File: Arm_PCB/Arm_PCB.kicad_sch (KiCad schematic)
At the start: 29 parts, among them J1 Conn_02x02_Counter_Clockwise, J10 Conn_02x04_Counter_Clockwise, J11 Conn_02x04_Counter_Clockwise, J2 Conn_02x03_Counter_Clockwise, J3 Conn_02x07_Counter_Clockwise, J4 Conn_02x05_Counter_Clockwise, J5 Conn_02x04_Counter_Clockwise, J6 Conn_02x04_Counter_Clockwise, J7 Conn_02x04_Counter_Clockwise, J8 Conn_02x04_Counter_Clockwise, J9 Conn_02x02_Counter_Clockwise, SW0 SW_Push, SW1 SW_Push, SW2 SW_Push, SW3 SW_Push

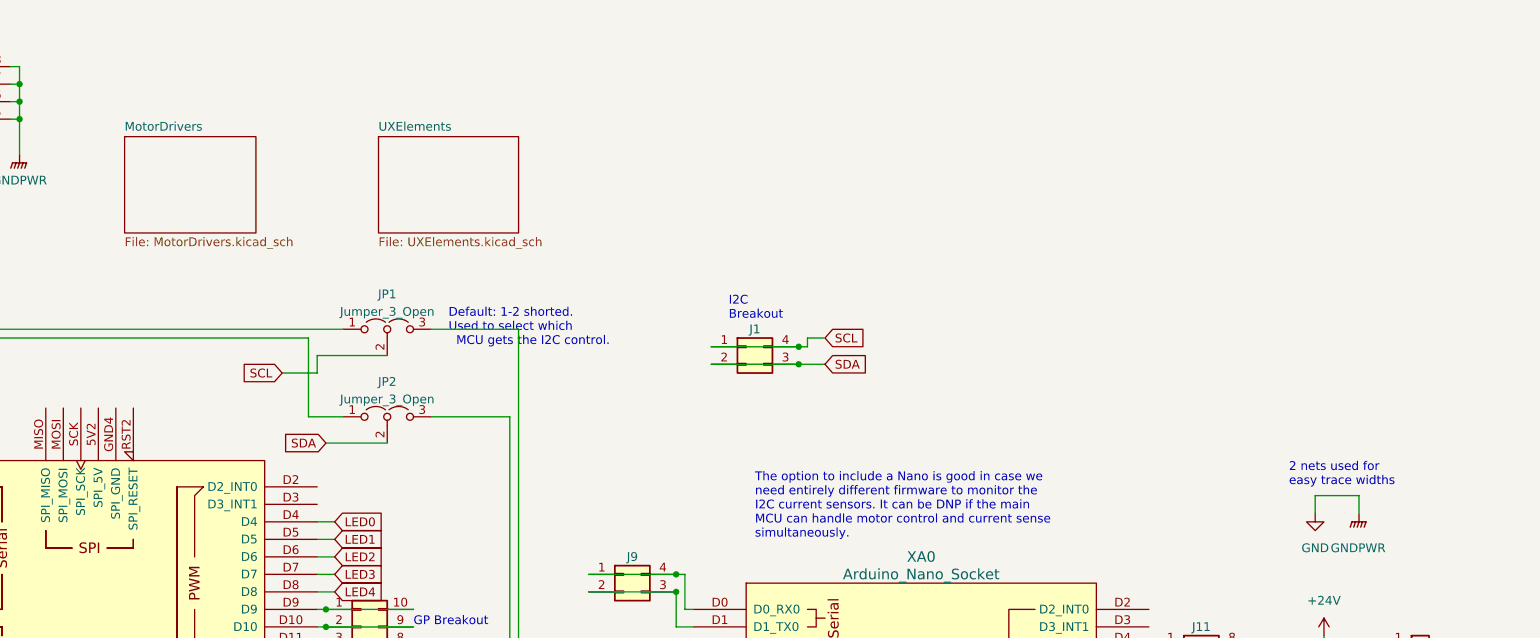
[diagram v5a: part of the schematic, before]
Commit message: Add servo current sensors, etc.
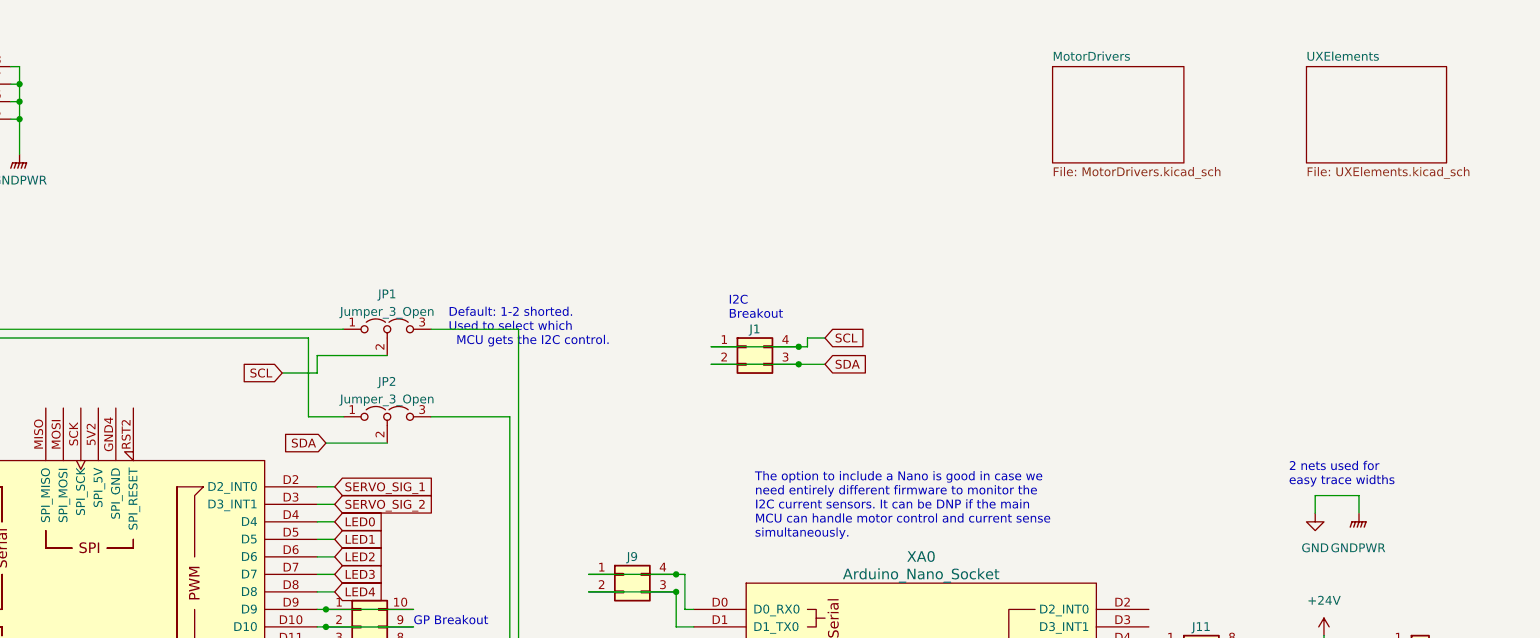
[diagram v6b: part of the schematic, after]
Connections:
- net SERVO_SIG_1: now reaches XA1.D2 (D2_INT0)
- net SERVO_SIG_2: now reaches XA1.D3 (D3_INT1)
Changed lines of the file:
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@@
+    (stroke (width 0) (type default))
+  )
+  (wire (pts (xy 93.98 82.55) (xy 96.52 82.55))
     (stroke (width 0) (type default))
   )
@@
   )
   (wire (pts (xy 13.97 87.63) (xy 26.67 87.63))
+    (stroke (width 0) (type default))
+  )
+  (wire (pts (xy 93.98 85.09) (xy 96.52 85.09))
     (stroke (width 0) (type default))
   )
@@
     (effects (font (size 1.27 1.27)) (justify left))
     (property "Intersheetrefs" "${INTERSHEET_REFS}" (at 105.0412 120.5706 0)
+      (effects (font (size 1.27 1.27)) (justify left) hide)
+    )
+  )
+  (global_label "SERVO_SIG_1" (shape input) (at 96.52 82.55 0) (fields_autoplaced)
+    (effects (font (size 1.27 1.27)) (justify left))
+    (property "Intersheetrefs" "${INTERSHEET_REFS}" (at 111.7024 82.55 0)
       (effects (font (size 1.27 1.27)) (justify left) hide)
     )
@@
     (effects (font (size 1.27 1.27)) (justify left))
     (property "Intersheetrefs" "${INTERSHEET_REFS}" (at 104.4364 118.0306 0)
+      (effects (font (size 1.27 1.27)) (justify left) hide)
+    )
+  )
+  (global_label "SERVO_SIG_2" (shape input) (at 96.52 85.09 0) (fields_autoplaced)
+    (effects (font (size 1.27 1.27)) (justify left))
+    (property "Intersheetrefs" "${INTERSHEET_REFS}" (at 111.7024 85.09 0)
       (effects (font (size 1.27 1.27)) (justify left) hide)
     )
@@
     )
   )
-  (sheet (at 102.87 31.75) (size 20.32 13.97) (fields_autoplaced)
+  (sheet (at 237.49 21.59) (size 20.32 13.97) (fields_autoplaced)
     (stroke (width 0.1524) (type solid))
     (fill (color 0 0 0 0.0000))
-    (property "Sheetname" "UXElements" (at 102.87 31.0384 0)
+    (property "Sheetname" "UXElements" (at 237.49 20.8784 0)
       (effects (font (size 1.27 1.27)) (justify left bottom))
     )
-    (property "Sheetfile" "UXElements.kicad_sch" (at 102.87 46.3046 0)
+    (property "Sheetfile" "UXElements.kicad_sch" (at 237.49 36.1446 0)
       (effects (font (size 1.27 1.27)) (justify left top))
     )
@@
     )
   )
-  (sheet (at 66.04 31.75) (size 19.05 13.97) (fields_autoplaced)
+  (sheet (at 200.66 21.59) (size 19.05 13.97) (fields_autoplaced)
     (stroke (width 0.1524) (type solid))
     (fill (color 0 0 0 0.0000))
-    (property "Sheetname" "MotorDrivers" (at 66.04 31.0384 0)
+    (property "Sheetname" "MotorDrivers" (at 200.66 20.8784 0)
       (effects (font (size 1.27 1.27)) (justify left bottom))
     )
-    (property "Sheetfile" "MotorDrivers.kicad_sch" (at 66.04 46.3046 0)
+    (property "Sheetfile" "MotorDrivers.kicad_sch" (at 200.66 36.1446 0)
       (effects (font (size 1.27 1.27)) (justify left top))
     )

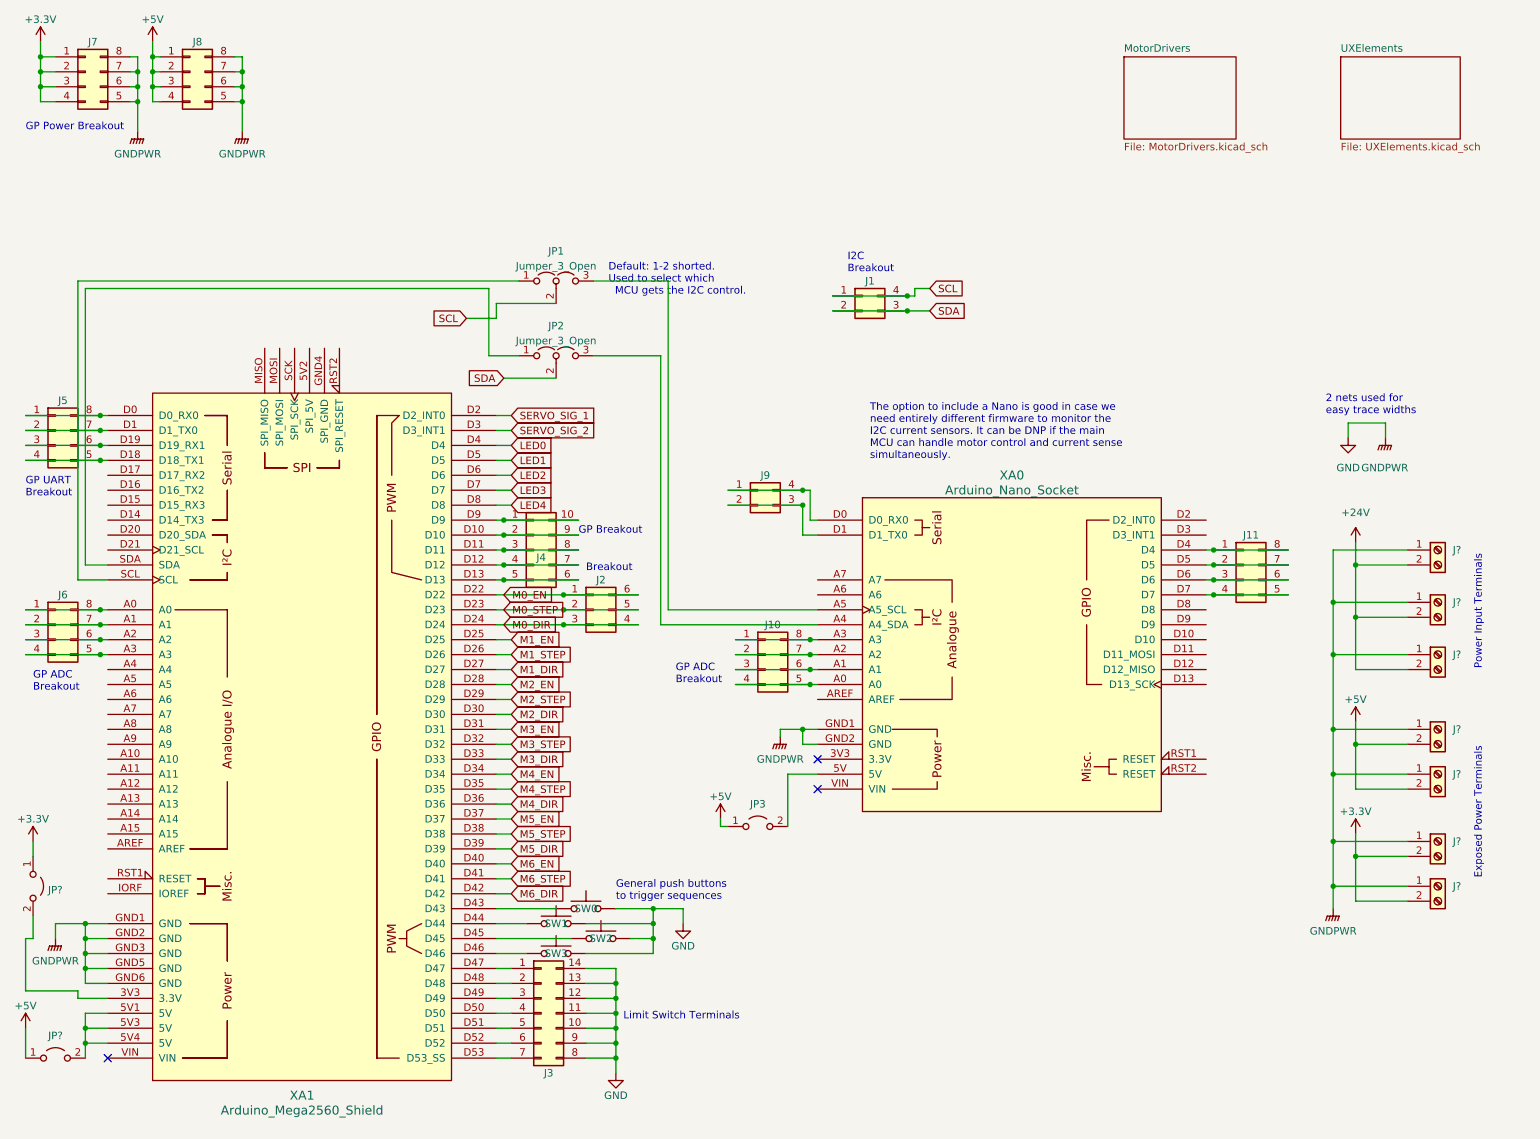
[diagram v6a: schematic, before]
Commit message: Annotate all pages
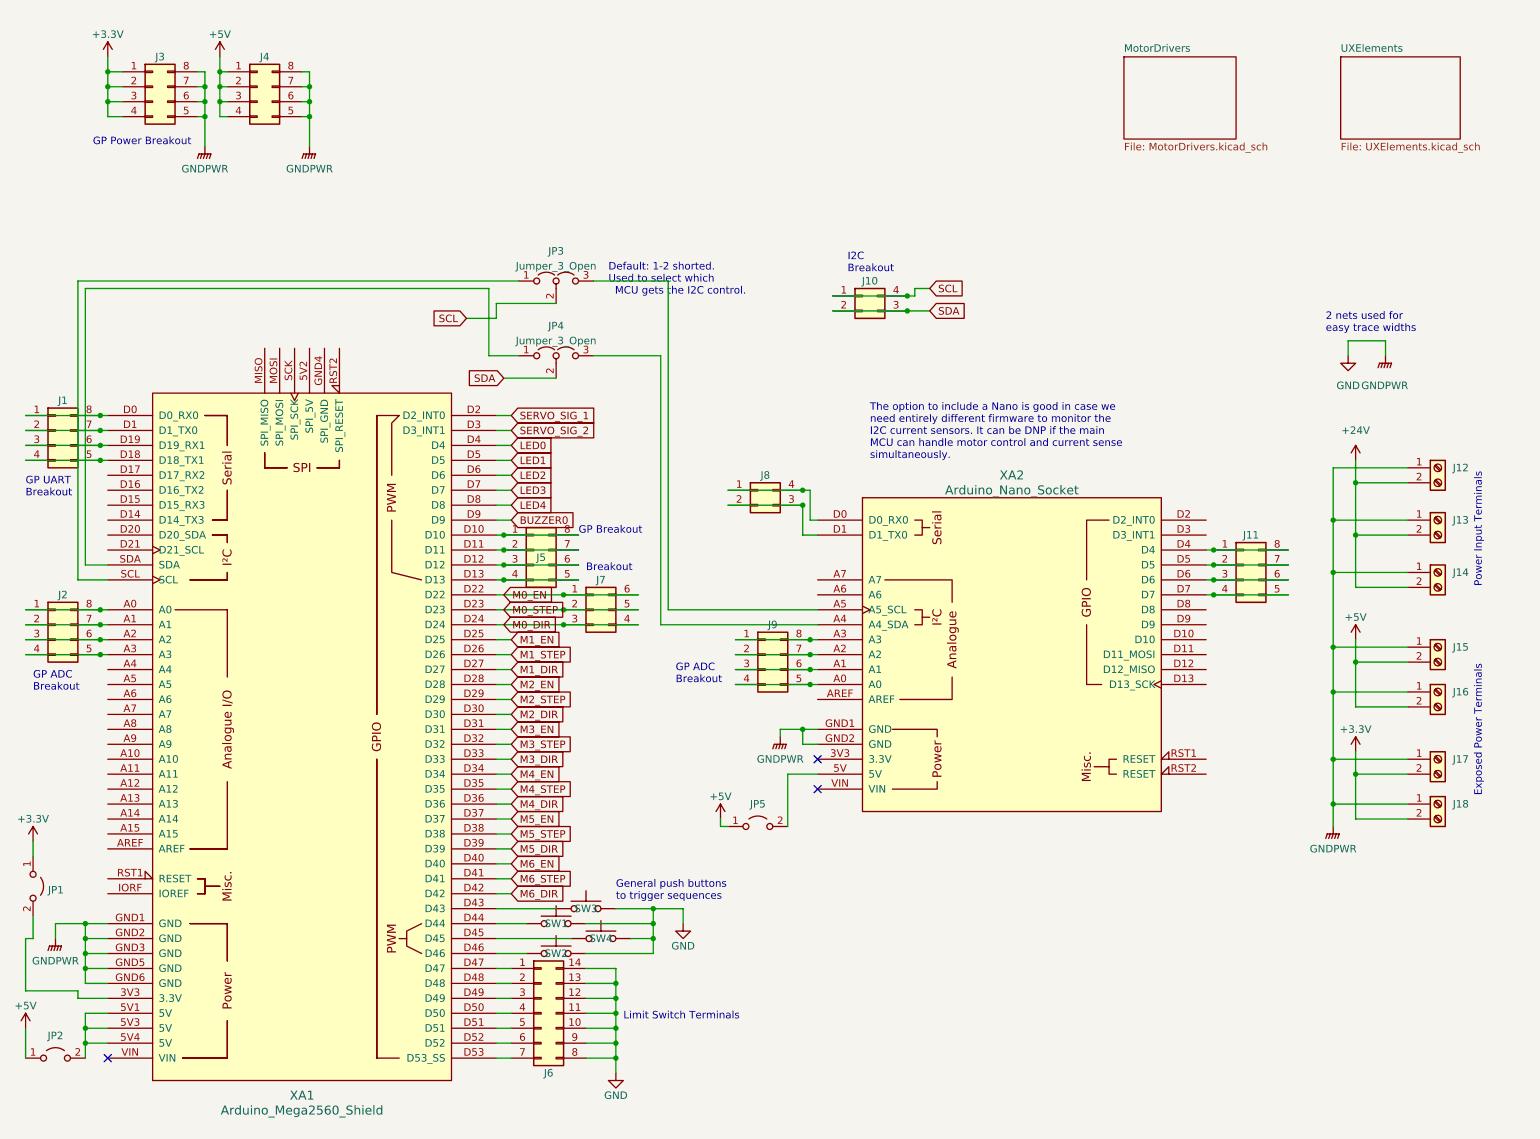
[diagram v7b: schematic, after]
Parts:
- J5: renamed from J4; symbol Connector_Generic:Conn_02x05_Counter_Clockwise -> Connector_Generic:Conn_02x04_Counter_Clockwise
- gave numbers to parts that had none: 9
- renumbered J5 to J1, J1 to J10, J6 to J2, J7 to J3, J8 to J4, J3 to J6, J2 to J7, J9 to J8, J10 to J9, JP1 to JP3, JP2 to JP4, JP3 to JP5, SW3 to SW2, SW0 to SW3, SW2 to SW4, XA0 to XA2
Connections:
- net at J5.5 (Pin_5), XA1.D13: now also J5.4 (Pin_4); no longer J5.6 (Pin_6)
- new net: J5.1 (Pin_1), J5.8 (Pin_8), XA1.D10
- new net: J5.2 (Pin_2), J5.7 (Pin_7), XA1.D11
- new net: J5.3 (Pin_3), J5.6 (Pin_6), XA1.D12
- new net BUZZER0: XA1.D9
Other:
- moved on the sheet: J12, J13, J14, J15, J16, J17, J18, J3, J4
